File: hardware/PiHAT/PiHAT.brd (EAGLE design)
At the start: 65 x 56.5 mm, 1 part

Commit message: Bulk copy/paste schematic
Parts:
- added C1, C16, C17, C6, C9: 1uF, SparkFun-Capacitors:0805
- added C10, C11: 0.1uF, SparkFun-Capacitors:0805
- added C12, C13, C14, C15, C3, C4, C5, C7: 0.1uF, SparkFun-Passives:0805
- added C2: 100pF, SparkFun-Capacitors:0805
- added C8: 4.7uF, SparkFun-Capacitors:0805
- added IAQ-CORE: IAQ-CORE, IAQ-CORE:IAQ-CORE
- added J2: (no value), SparkFun-Connectors:AVR_ICSP
- added J3: USB-MICROB, SparkFun-Connectors:USB-MICROB
- added LED2, RX, TX: (no value), adafruit:CHIPLED_0805
- added MICS4514: SPARKFUN-SENSORS_MICS-4514, MICS-4514_CO_and_NOx_Sensor_Breakout:SPARKFUN-SENSORS_MICS_10-SMD
- added MOSFET: SPARKFUN-DISCRETESEMI_MOSFET-NCHANNELBSS138, MICS-4514_CO_and_NOx_Sensor_Breakout:SPARKFUN-DISCRETESEMI_SOT23-3
- added R1, R13, R7: 10K, SparkFun-Passives:0805
- added R10, R9: 47, SparkFun-Passives:0805
- added R11: SHOTTKY, SparkFun-Passives:0805
- added R12, R21: 27, SparkFun-Passives:0805
- added R14: 47K, SparkFun-Passives:0805
- added R15, R18: 82, SparkFun-Passives:0805
- added R16: 22K, SparkFun-Passives:0805
- added R17: 51, SparkFun-Passives:0805
- added R19, R8: 100K, SparkFun-Passives:0805
- added R20: 100, SparkFun-Passives:0805
- added R3: 1.5K, SparkFun-Passives:0805
- added R4: 47, SparkFun-Resistors:0805
- added R5, R6: 10K, SparkFun-Resistors:0805
- added RESET: TAC_SWITCHSMD, SparkFun-Retired:TACTILE-SWITCH-SMD
- added U$3: OPA344, SparkFun-AnalogIC:SOT23-5
- added U$4: RFM69HW, RFM69 USB Gateway:LOWPOWERLAB_RFM69W-MINPADS
- added U1: ATMEGA328P, SparkFun-DigitalIC:TQFP32-08
- added U2: TSL2561, SparkFun-DigitalIC:FN-6
- added U4: MPL115A, SparkFun-Sensors:LGA8
- added U5: FT231XS, SparkFun-DigitalIC:SSOP20_L
- added U6: ADMP401, SparkFun-Sensors:ADMP401
- added U7: SHT31-DIS, thomasb9511:SHT3X
- added U8, U9: MCP1703CB, linear:SOT23
- added X1: (no value), adafruit:SMA_EDGELAUNCH
- added Y1: 16MHZ, SparkFun-FreqCtrl:RESONATOR-SMD
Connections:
- new net 5V: C17.1, C7.1, MICS4514.F, MICS4514.G, MICS4514.H, MICS4514.J, U9.2
- new net A0: C2.2, R8.1, U$3.1, U1.23
- new net A7: U1.22
- new net ANT: U$4.ANA, X1.P
- new net D2: U$4.DIO0, U1.32
- new net D5: U1.9
- new net DTR: C12.1, J2.10, U5.1
- new net FTDI_VCC: R10.1, R9.1, U5.13, U5.14, U5.3
- new net MISO: J2.1, U$4.MISO, U1.16
- new net MOSI: J2.4, U$4.MOSI, U1.15
- new net N$10: C2.1, R3.1, R8.2, U$3.4
- new net N$11: C9.1, R1.2, R7.1, U$3.3
- new net N$12: C13.1, U4.2
- new net N$13: MICS4514.C, R15.2
- new net N$17: RX.C, U5.17
- new net N$18: TX.C, U5.10
- new net N$2: R4.1, U1.13
- new net N$20: MOSFET.3, R17.2, R18.1
- new net N$23: MOSFET.1, R19.2, R20.1
- new net N$25: R21.1, U5.12
- new net N$26: R12.1, U5.11
- new net N$27: R9.2, RX.A
- new net N$29: R10.2, TX.A
- new net N$3: LED2.A, R4.2
- new net N$32: J3.D-, R21.2
- new net N$33: J3.D+, R12.2
- new net N$4: U1.8, Y1.3
- new net N$5: U1.7, Y1.1
- new net N$7: C8.1, U6.1
- new net N$8: MICS4514.A, R18.2
- new net N$9: C8.2, R3.2
- new net PRE: R20.2, U1.1
- new net PWR: C1.1, C16.1, J2.2, R11.1, U8.3, U9.3
- new net RESET: C12.2, J2.5, R13.1, RESET.3, RESET.4, U1.29
- new net RX: J2.7, U1.30, U5.20
- new net SCK: J2.3, U$4.SCK, U1.17
- new net SS: J2.9, U$4.NSS, U1.14
- new net TX: J2.8, U1.31, U5.4
- new net VBUS: C11.1, J3.VBUS, R11.2, U5.15
- new net VCC: C10.1, C14.1, C15.1, C3.1, C4.1, C5.1, C6.1, IAQ-CORE.VCC, R13.2, R5.2, R6.2, R7.2, U$3.5, U$4.VDD, U1.18, U1.4, U1.6, U2.1, U4.1, U4.4, U6.5, U7.P$5, U8.2
- new net VNOX: MICS4514.B, R16.2, U1.24
- new net VRED: MICS4514.D, R14.2, U1.25
- net GND: now also C1.2, C10.2, C11.2, C13.2, C14.2, C15.2, C16.2, C17.2, C3.2, C4.2, C5.2, C6.2, C7.2, C9.2, IAQ-CORE.GND, J2.6, J3.GND, J3.MT1, J3.MT2, LED2.C, MOSFET.2, R1.1, R14.1, R15.1, R16.1, R17.1, R19.1, RESET.1, RESET.2, U$3.2, U$4.GND, U1.21, U1.3, U1.5, U2.3, U4.3, U5.16, U5.6, U6.2, U6.4, U6.6, U7.P$2, U7.P$7, U7.P$8, U7.PAD, U8.1, U9.1, X1.GND@1, X1.GND@2, X1.GND@3, X1.GND@4, Y1.2
- net SCL: now also IAQ-CORE.SCL, R6.1, U1.28, U2.4, U4.8, U7.P$4
- net SDA: now also IAQ-CORE.SDA, R5.1, U1.27, U2.6, U4.7, U7.P$1

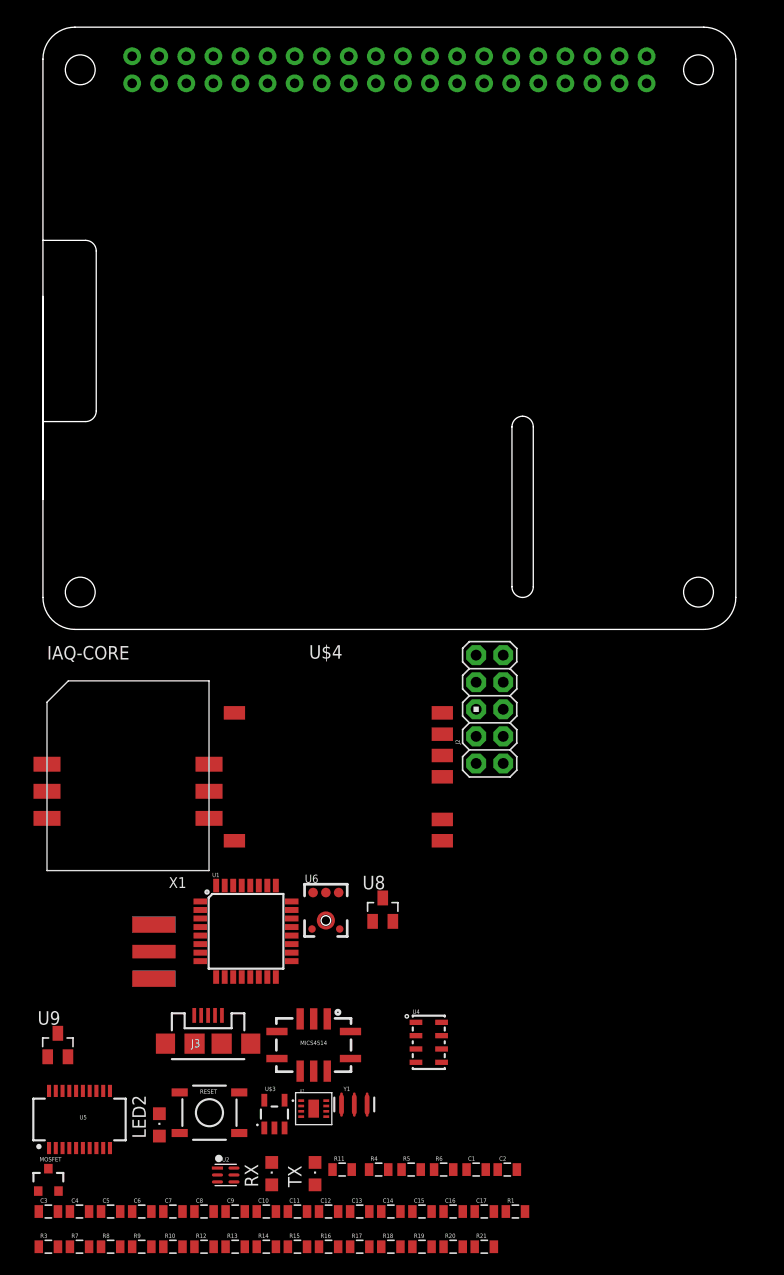
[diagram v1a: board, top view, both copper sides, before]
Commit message: Removed FTDI, RFM69, USB
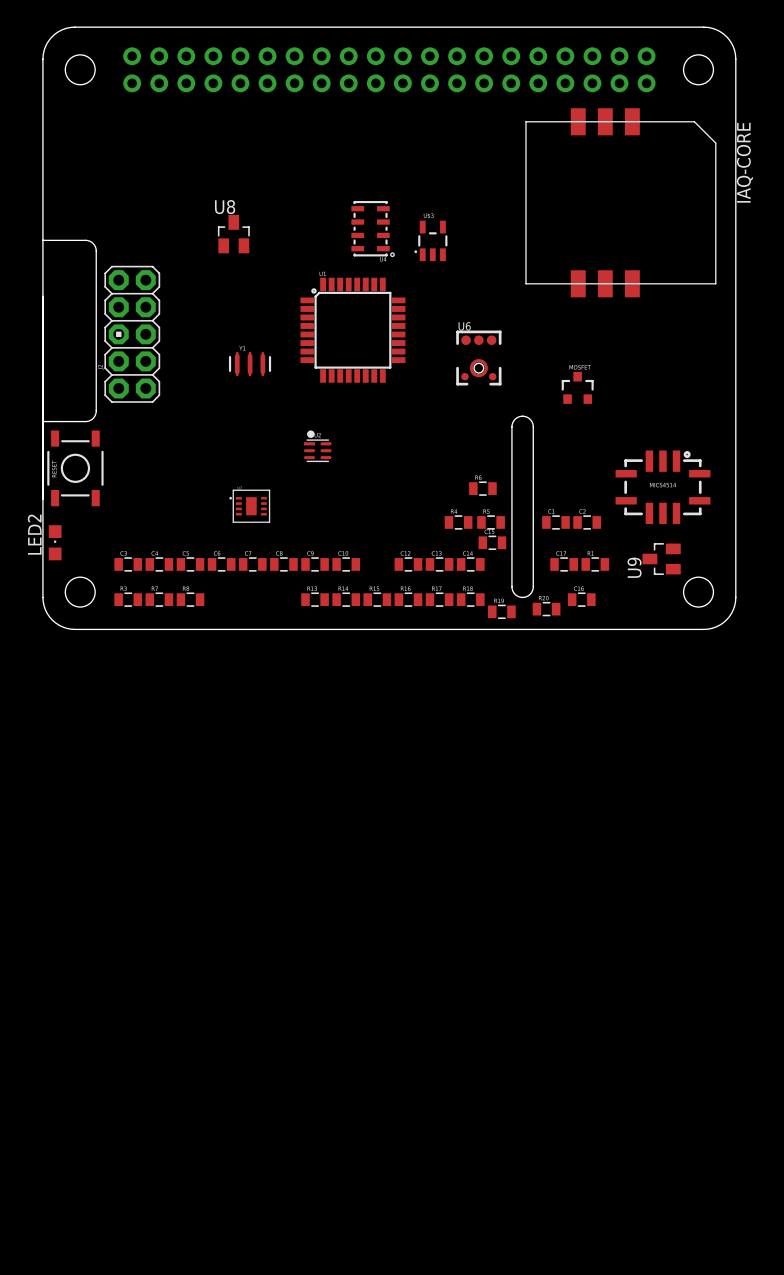
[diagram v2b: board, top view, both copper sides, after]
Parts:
- removed C11: 0.1uF, SparkFun-Capacitors:0805
- removed J3: USB-MICROB, SparkFun-Connectors:USB-MICROB
- removed R10, R9: 47, SparkFun-Passives:0805
- removed R11: SHOTTKY, SparkFun-Passives:0805
- removed R12, R21: 27, SparkFun-Passives:0805
- removed RX, TX: (no value), adafruit:CHIPLED_0805
- removed U$4: RFM69HW, RFM69 USB Gateway:LOWPOWERLAB_RFM69W-MINPADS
- removed U5: FT231XS, SparkFun-DigitalIC:SSOP20_L
- removed X1: (no value), adafruit:SMA_EDGELAUNCH
- moved MOSFET 89.4 mm to (50.2, 21.3)
- moved U$3 83.3 mm to (36.6, 35.2)
- moved IAQ-CORE 81.8 mm to (63.1, 46.4), turned to 270 degrees
- moved U4 76.5 mm to (30.7, 36.3), turned to 180 degrees
- moved U9 72.7 mm to (58.0, 5.33), turned to 90 degrees
- moved Y1 70.2 mm to (19.4, 23.6)
- moved U2 68.5 mm to (25.8, 15.5)
- moved U8 64.9 mm to (17.9, 35.8)
- moved R6 64.0 mm to (41.3, 11.9)
- moved C15 63.1 mm to (42.2, 6.86)
- moved RESET 61.7 mm to (3.05, 13.8), turned to 90 degrees
- moved MICS4514 61.7 mm to (58.2, 12.1)
- moved C10 61.2 mm to (28.4, 4.83)
- moved C12 61.2 mm to (34.3, 4.83)
- moved C13 61.2 mm to (37.2, 4.83)
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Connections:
- removed net ANT: U$4.ANA, X1.P
- removed net FTDI_VCC: R10.1, R9.1, U5.13, U5.14, U5.3
- removed net N$17: RX.C, U5.17
- removed net N$18: TX.C, U5.10
- removed net N$25: R21.1, U5.12
- removed net N$26: R12.1, U5.11
- removed net N$27: R9.2, RX.A
- removed net N$29: R10.2, TX.A
- removed net N$32: J3.D-, R21.2
- removed net N$33: J3.D+, R12.2
- removed net VBUS: C11.1, J3.VBUS, R11.2, U5.15
- net D2: no longer U$4.DIO0
- net DTR: no longer U5.1
- net GND: no longer C11.2, J3.GND, J3.MT1, J3.MT2, U$4.GND, U5.16, U5.6, X1.GND@1, X1.GND@2, X1.GND@3, X1.GND@4
- net MISO: no longer U$4.MISO
- net MOSI: no longer U$4.MOSI
- net PWR: no longer R11.1
- net RX: no longer U5.20
- net SCK: no longer U$4.SCK
- net SS: no longer U$4.NSS
- net TX: no longer U5.4
- net VCC: no longer U$4.VDD

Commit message: started mapping sensors for pi hat
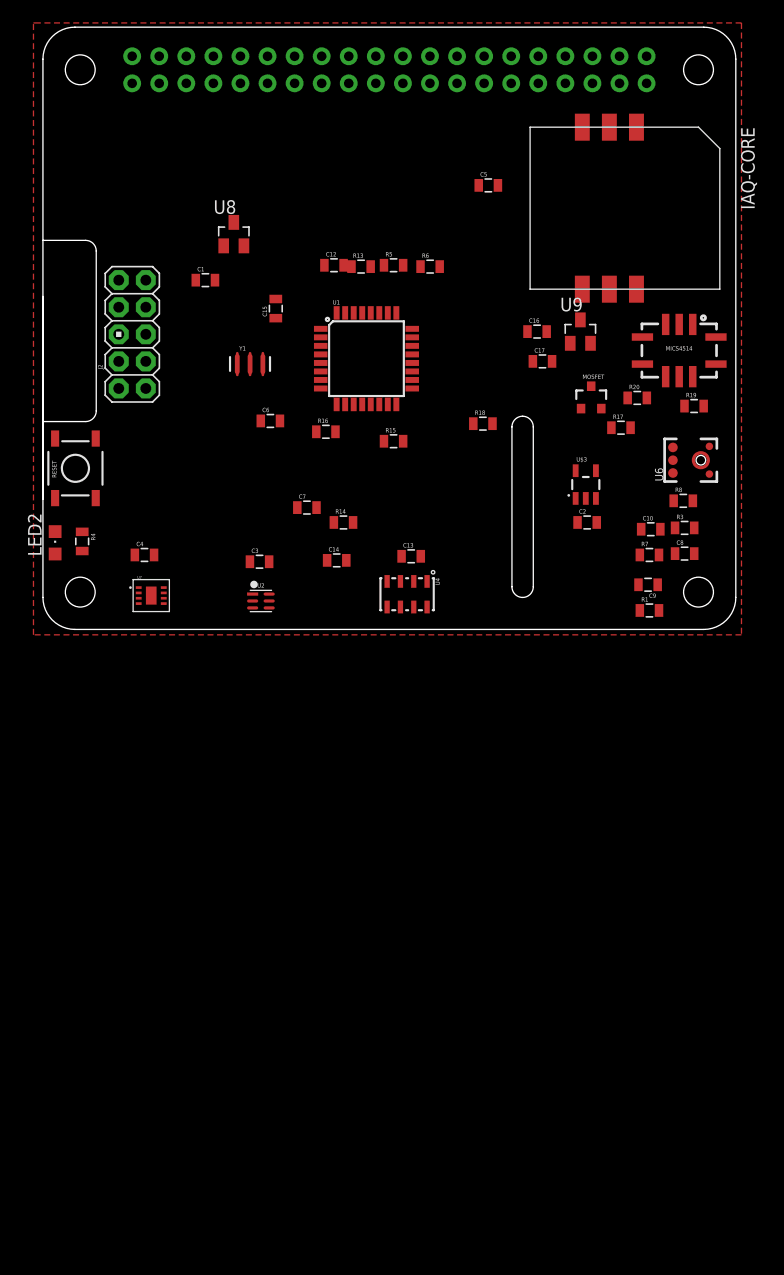
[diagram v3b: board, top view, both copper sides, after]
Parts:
- moved R3 52.6 mm to (60.2, 8.26)
- moved R8 47.1 mm to (60.1, 10.8)
- moved R7 46.2 mm to (56.9, 5.71)
- moved C5 45.2 mm to (41.8, 40.4)
- moved C1 40.0 mm to (15.2, 31.5)
- moved C8 37.6 mm to (60.2, 5.84)
- moved R4 35.4 mm to (3.68, 6.99), turned to 270 degrees
- moved U4 34.5 mm to (34.2, 2.03), turned to 270 degrees
- moved R13 31.5 mm to (29.8, 32.8)
- moved C9 31.3 mm to (56.8, 2.92), turned to 180 degrees
- moved C15 29.9 mm to (21.8, 28.8), turned to 90 degrees
- moved C12 28.9 mm to (27.3, 32.9)
- moved C10 28.8 mm to (57.0, 8.13)
- moved U$3 27.0 mm to (50.9, 12.3)
- moved R19 26.4 mm to (61.1, 19.7)
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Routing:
- added copper zone on layer 1, net GND

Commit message: All traces routed - v0.1
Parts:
- removed C1, C16, C17, C6: 1uF, SparkFun-Capacitors:0805
- removed U8, U9: MCP1703CB, linear:SOT23
- moved R14 46.7 mm to (58.8, 44.0), turned to 180 degrees
- moved R16 40.1 mm to (62.0, 36.1), turned to 90 degrees
- moved C7 38.7 mm to (51.6, 38.0), turned to 270 degrees
- moved R4 37.5 mm to (1.65, 44.5)
- moved R15 37.3 mm to (62.0, 39.8), turned to 270 degrees
- moved LED2 32.6 mm to (1.65, 39.5), turned to 180 degrees
- moved R13 26.4 mm to (8.26, 17.6), turned to 270 degrees
- moved C12 22.1 mm to (11.3, 17.6), turned to 270 degrees
- moved R18 20.6 mm to (59.1, 28.4), turned to 90 degrees
- moved R5 18.8 mm to (36.1, 14.4)
- moved IAQ-CORE 16.4 mm to (47.1, 45.2)
- moved R6 15.8 mm to (36.1, 17.0)
- moved C5 13.9 mm to (40.2, 26.5)
- moved R17 13.1 mm to (61.6, 28.4), turned to 270 degrees
- moved MICS4514 13.1 mm to (56.6, 37.6), turned to 270 degrees
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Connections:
- removed net 3.3V: RPI1.1, RPI1.17
- removed net 5.0V: RPI1.2, RPI1.4
- net 5V: now also RPI1.2, RPI1.4; no longer C17.1, U9.2
- net GND: no longer C1.2, C16.2, C17.2, C6.2, U8.1, U9.1
- net PWR: no longer C1.1, C16.1, U8.3, U9.3
- net VCC: now also RPI1.1, RPI1.17; no longer C6.1, U8.2
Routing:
- net VCC: track 0.00 -> 193.5 mm, vias 0 -> 2
- net SCL: track 0.00 -> 129.9 mm, vias 0 -> 5
- net SDA: track 0.00 -> 111.8 mm, vias 0 -> 6
- net 5V: track 0.00 -> 72.8 mm
- net A0: track 0.00 -> 68.8 mm, vias 0 -> 3
- net VRED: track 0.00 -> 63.7 mm, vias 0 -> 2
- net VNOX: track 0.00 -> 57.5 mm, vias 0 -> 2
- net RESET: track 0.00 -> 55.8 mm, vias 0 -> 2
- net N$2: track 0.00 -> 43.3 mm, vias 0 -> 2
- net SCK: track 0.00 -> 36.2 mm, vias 0 -> 1
- net MISO: track 0.00 -> 31.9 mm, vias 0 -> 1
- net TX: track 0.00 -> 30.8 mm, vias 0 -> 2
- net RX: track 0.00 -> 27.0 mm, vias 0 -> 2
- net MOSI: track 0.00 -> 26.4 mm, vias 0 -> 2
- net PRE: track 0.00 -> 23.9 mm
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- added copper zone on layer 16, net GND

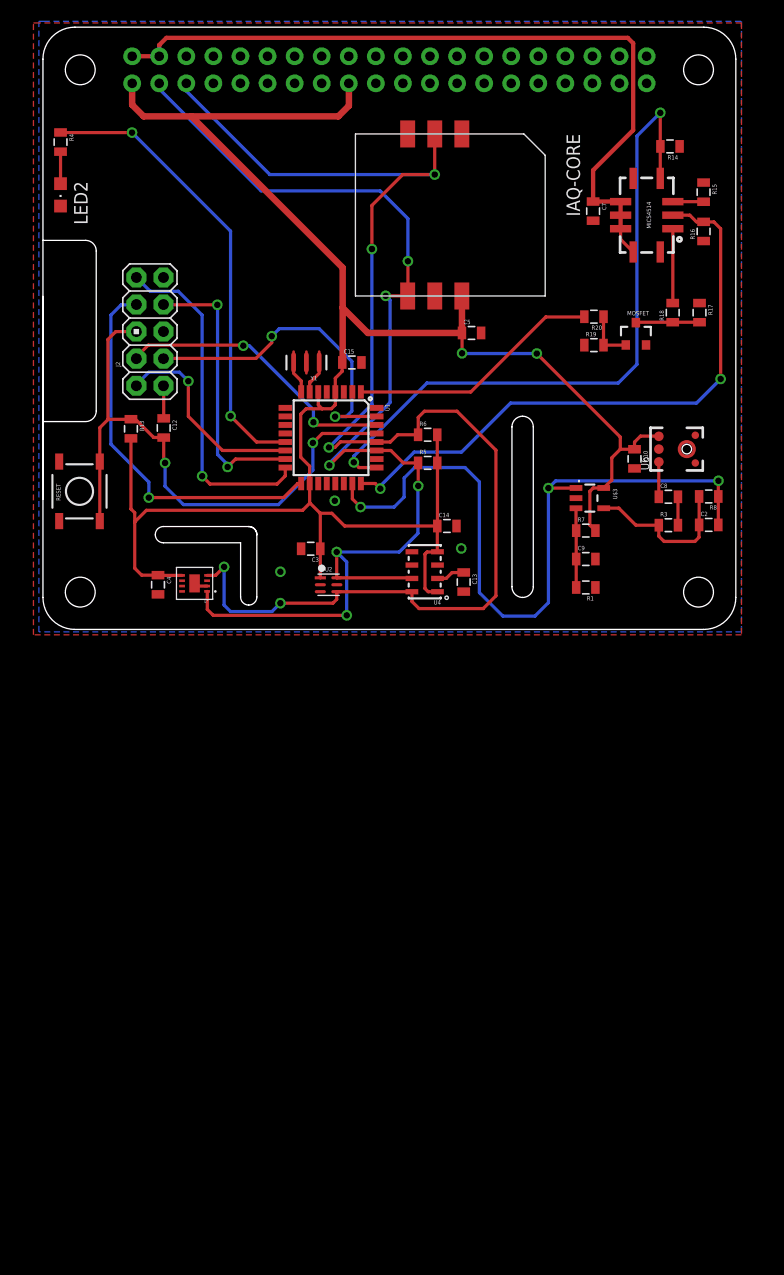
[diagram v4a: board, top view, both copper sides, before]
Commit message: Fixed several traces
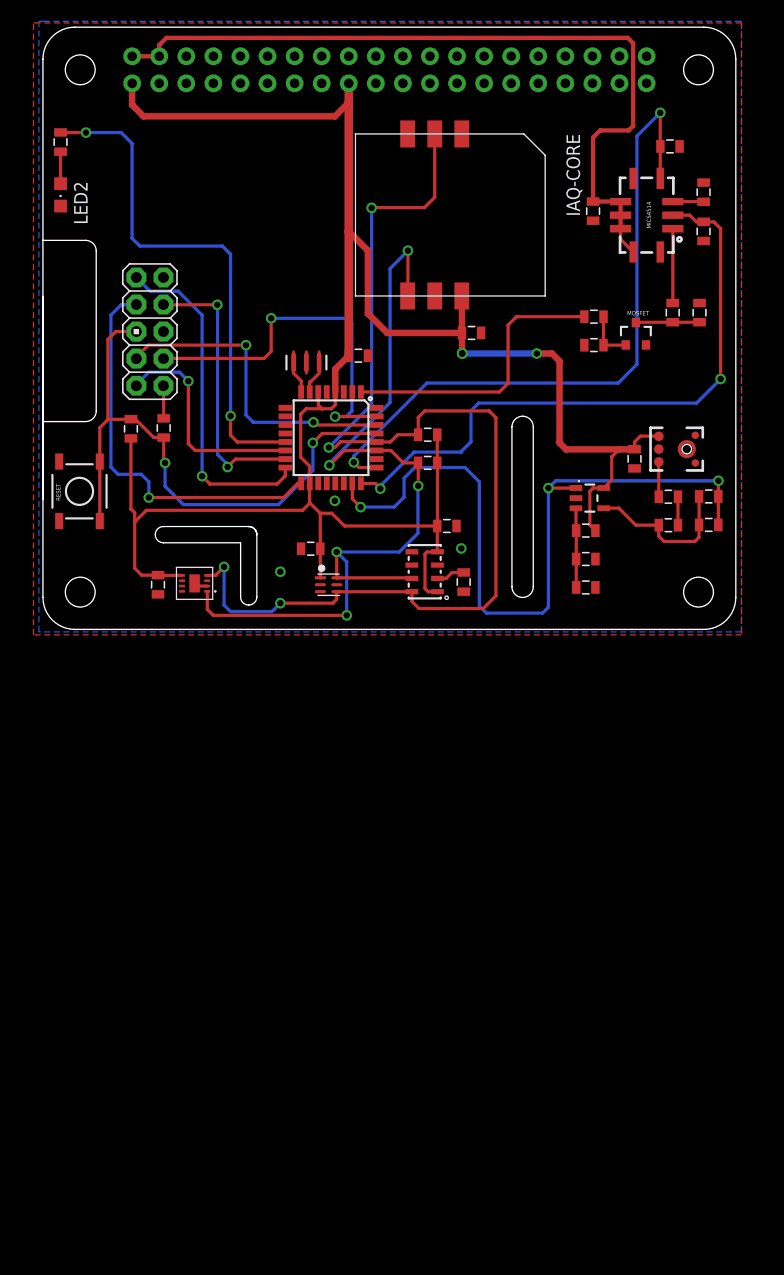
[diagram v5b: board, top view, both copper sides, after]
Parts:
- moved C15 0.88 mm to (29.6, 24.4)
- renumbered U$3 to U3
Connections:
- new net PI_SCL: RPI1.5
- new net PI_SDA: RPI1.3
- net SCL: no longer RPI1.5
- net SDA: no longer RPI1.3
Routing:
- net SDA: track 111.8 -> 82.7 mm, vias 6 -> 5
- net SCL: track 129.9 -> 105.6 mm, vias 5 -> 4
- net VCC: track 193.5 -> 198.5 mm, vias 2 -> 3
- net N$2: track 43.3 -> 48.3 mm
- net TX: track 30.8 -> 35.2 mm
- net PRE: track 23.9 -> 27.1 mm
- net RX: track 27.0 -> 30.1 mm
- net VNOX: track 57.5 -> 59.2 mm
- net 5V: track 72.8 -> 74.3 mm
- net SS: track 19.5 -> 21.0 mm
- net SCK: track 36.2 -> 37.5 mm
- net A0: track 68.8 -> 69.6 mm

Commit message: Added labels
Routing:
- net SDA: track 82.7 -> 85.3 mm
- net N$2: track 48.3 -> 50.6 mm
- net A0: track 69.6 -> 71.4 mm
- net VNOX: track 59.2 -> 60.8 mm
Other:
- board text added: "Status LED"
